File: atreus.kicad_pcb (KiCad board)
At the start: 2 copper layers, 111.8 x 87.6 mm, 45 parts

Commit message: Programmatically place repeated traces.
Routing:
- net N-row-2: track 173.4 -> 149.4 mm
- net N-diode-22: track 0.00 -> 18.8 mm
- net N-diode-20: track 14.1 -> 0.00 mm
- net N-diode-23: track 0.00 -> 13.5 mm
- net N-diode-21: track 12.0 -> 0.00 mm
- net N-col-4: track 119.4 -> 130.7 mm
- net N-col-1: track 182.1 -> 193.1 mm
- net N-col-5: track 67.0 -> 56.7 mm
- net N-col-0: track 207.2 -> 214.9 mm
- net N-row-0: track 132.1 -> 138.5 mm
- net N-col-3: track 155.4 -> 159.7 mm
- net N-row-1: track 121.1 -> 124.1 mm
- net N-col-2: track 177.2 -> 179.5 mm

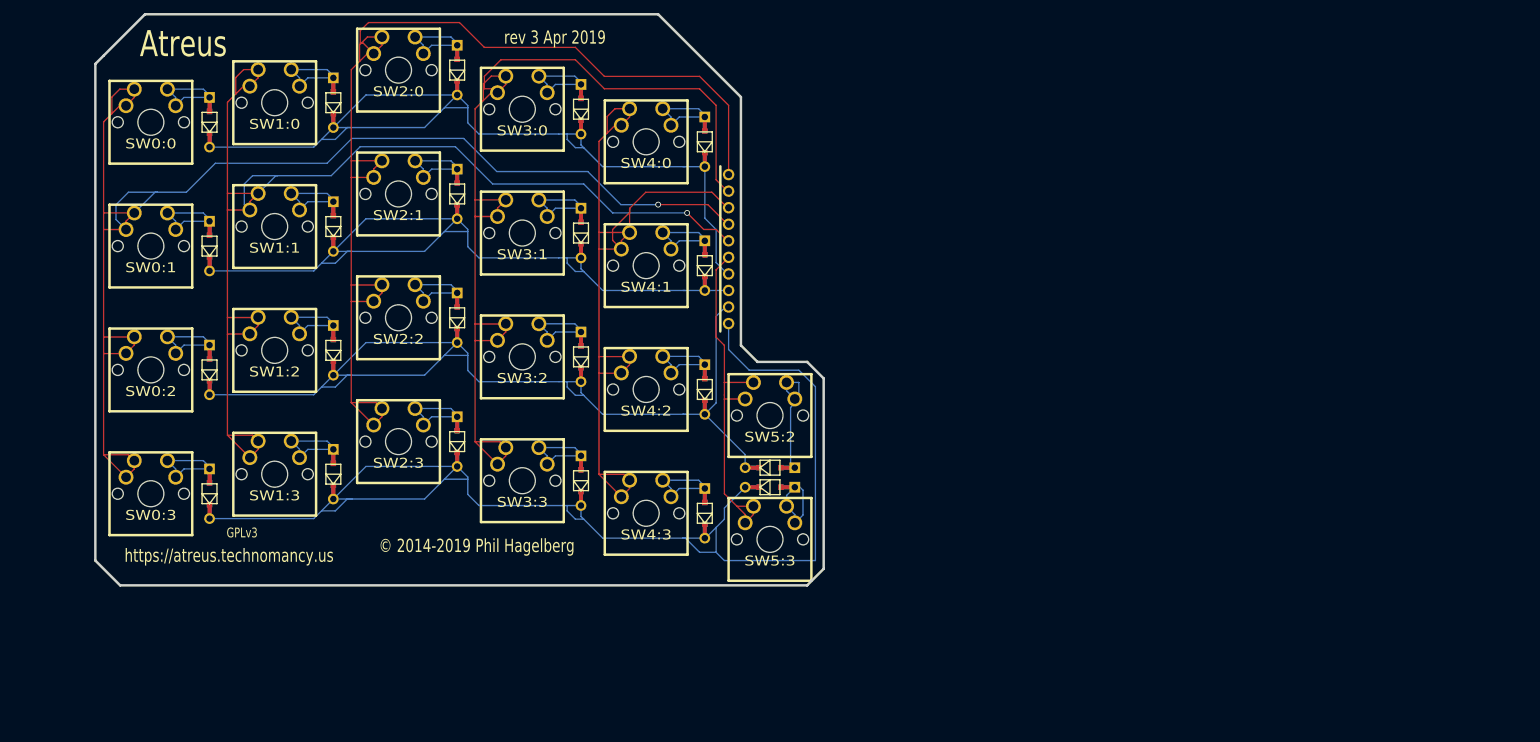
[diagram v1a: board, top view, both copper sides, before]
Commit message: Revert changes to create split PCB.
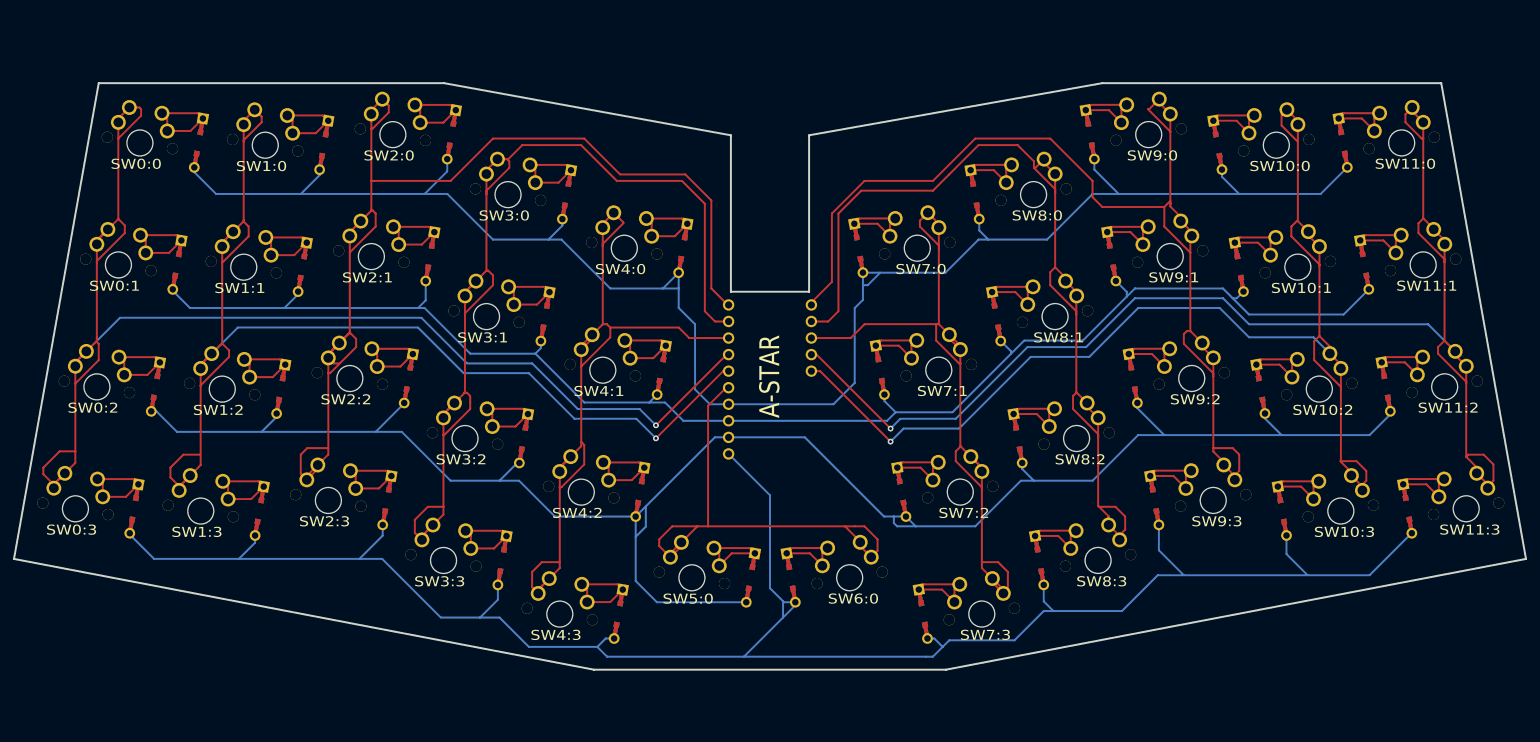
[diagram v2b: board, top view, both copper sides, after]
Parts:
- removed the D2:2 at (48.0, 28.0)
- removed the D2:2 at (86.0, 39.0)
- removed the D2:2 at (86.0, 58.0)
- removed the D2:2 at (86.0, 77.0)
- removed the D2:2 at (105.0, 26.0)
- removed the D2:2 at (105.0, 45.0)
- removed the D2:2 at (105.0, 64.0)
- removed the D2:2 at (105.0, 83.0)
- removed the D2:2 at (124.0, 31.0)
- removed the D2:2 at (124.0, 50.0)
- removed the D2:2 at (124.0, 69.0)
- removed the D2:2 at (48.0, 47.0)
- removed the D2:2 at (124.0, 88.0)
- removed the D2:2 at (134.0, 81.0)
- removed the D2:2 at (134.0, 84.0)
- removed the D2:2 at (48.0, 66.0)
- removed the D2:2 at (48.0, 85.0)
- removed the D2:2 at (67.0, 25.0)
- removed the D2:2 at (67.0, 44.0)
- removed the D2:2 at (67.0, 63.0)
- removed the D2:2 at (67.0, 82.0)
- removed the D2:2 at (86.0, 20.0)
- removed SW5:2, SW5:3: , MX_FLIP
- added D2:2: , DIODE, F.Cu at (46.3, 31.2)
- added D2:2: , DIODE, F.Cu at (81.8, 48.6)
- added D2:2: , DIODE, F.Cu at (78.5, 67.3)
- added D2:2: , DIODE, F.Cu at (75.2, 86.0)
- added D2:2: , DIODE, F.Cu at (102.8, 39.1)
- added D2:2: , DIODE, F.Cu at (99.5, 57.8)
- added D2:2: , DIODE, F.Cu at (96.2, 76.5)
- added D2:2: , DIODE, F.Cu at (92.9, 95.2)
- added D2:2: , DIODE, F.Cu at (120.6, 47.3)
- added D2:2: , DIODE, F.Cu at (117.3, 66.0)
- added D2:2: , DIODE, F.Cu at (114.0, 84.8)
- added D2:2: , DIODE, F.Cu at (43.0, 49.9)
- added D2:2: , DIODE, F.Cu at (110.7, 103.5)
- added D2:2: , DIODE, F.Cu at (131.0, 97.9)
- added D2:2: , DIODE, F.Cu at (137.2, 97.9)
- added D2:2: , DIODE, F.Cu at (147.6, 47.3)
- added D2:2: , DIODE, F.Cu at (150.9, 66.0)
- added D2:2: , DIODE, F.Cu at (154.2, 84.7)
- added D2:2: , DIODE, F.Cu at (157.5, 103.5)
- added D2:2: , DIODE, F.Cu at (165.4, 39.1)
- added D2:2: , DIODE, F.Cu at (168.7, 57.8)
- added D2:2: , DIODE, F.Cu at (172.0, 76.5)
- added D2:2: , DIODE, F.Cu at (39.7, 68.6)
- added D2:2: , DIODE, F.Cu at (175.3, 95.2)
- added D2:2: , DIODE, F.Cu at (183.1, 29.9)
- added D2:2: , DIODE, F.Cu at (186.4, 48.6)
- added D2:2: , DIODE, F.Cu at (189.7, 67.3)
- added D2:2: , DIODE, F.Cu at (193.0, 86.0)
- added D2:2: , DIODE, F.Cu at (202.7, 31.5)
- added D2:2: , DIODE, F.Cu at (206.0, 50.2)
- added D2:2: , DIODE, F.Cu at (209.3, 68.9)
- added D2:2: , DIODE, F.Cu at (212.6, 87.7)
- added D2:2: , DIODE, F.Cu at (221.9, 31.2)
- added D2:2: , DIODE, F.Cu at (36.4, 87.3)
- added D2:2: , DIODE, F.Cu at (225.2, 49.9)
- added D2:2: , DIODE, F.Cu at (228.5, 68.6)
- added D2:2: , DIODE, F.Cu at (231.8, 87.3)
- added D2:2: , DIODE, F.Cu at (65.6, 31.5)
- added D2:2: , DIODE, F.Cu at (62.3, 50.2)
- added D2:2: , DIODE, F.Cu at (59.0, 68.9)
- added D2:2: , DIODE, F.Cu at (55.7, 87.7)
- added D2:2: , DIODE, F.Cu at (85.1, 29.9)
- added SW10:0: , MX_FLIP, F.Cu at (211.7, 31.5)
- added SW10:1: , MX_FLIP, F.Cu at (215.0, 50.2)
- added SW10:2: , MX_FLIP, F.Cu at (218.3, 68.9)
- added SW10:3: , MX_FLIP, F.Cu at (221.6, 87.7)
- added SW11:0: , MX_FLIP, F.Cu at (230.9, 31.2)
- added SW11:1: , MX_FLIP, F.Cu at (234.2, 49.9)
- added SW11:2: , MX_FLIP, F.Cu at (237.5, 68.6)
- added SW11:3: , MX_FLIP, F.Cu at (240.8, 87.3)
- added SW5:0: , MX_FLIP, F.Cu at (122.0, 97.9)
- added SW6:0: , MX_FLIP, F.Cu at (146.2, 97.9)
- added SW7:0: , MX_FLIP, F.Cu at (156.6, 47.3)
- added SW7:1: , MX_FLIP, F.Cu at (159.9, 66.0)
- added SW7:2: , MX_FLIP, F.Cu at (163.2, 84.7)
- added SW7:3: , MX_FLIP, F.Cu at (166.5, 103.5)
- added SW8:0: , MX_FLIP, F.Cu at (174.4, 39.1)
- added SW8:1: , MX_FLIP, F.Cu at (177.7, 57.8)
- added SW8:2: , MX_FLIP, F.Cu at (181.0, 76.5)
- added SW8:3: , MX_FLIP, F.Cu at (184.3, 95.2)
- added SW9:0: , MX_FLIP, F.Cu at (192.1, 29.9)
- added SW9:1: , MX_FLIP, F.Cu at (195.4, 48.6)
- added SW9:2: , MX_FLIP, F.Cu at (198.7, 67.3)
- added SW9:3: , MX_FLIP, F.Cu at (202.0, 86.0)
- ?: value (none) -> A-STAR
- moved SW4:3 20.4 mm to (101.7, 103.5), turned to -10 degrees
- moved ? 20.0 mm to (134.0, 70.0)
- moved SW4:2 18.6 mm to (105.0, 84.8), turned to -10 degrees
- moved SW4:1 17.4 mm to (108.3, 66.0), turned to -10 degrees
- moved SW3:3 17.2 mm to (83.9, 95.2), turned to -10 degrees
- moved SW4:0 16.7 mm to (111.6, 47.3), turned to -10 degrees
- moved SW3:2 15.3 mm to (87.2, 76.5), turned to -10 degrees
- moved SW2:3 14.1 mm to (66.2, 86.0), turned to -10 degrees
- moved SW3:1 13.9 mm to (90.5, 57.8), turned to -10 degrees
- moved SW3:0 13.3 mm to (93.8, 39.1), turned to -10 degrees
- moved SW1:3 12.7 mm to (46.7, 87.7), turned to -10 degrees
- moved SW2:2 11.9 mm to (69.5, 67.3), turned to -10 degrees
- moved SW0:3 11.8 mm to (27.4, 87.3), turned to -10 degrees
- moved SW2:1 10.5 mm to (72.8, 48.6), turned to -10 degrees
- moved SW1:2 10.0 mm to (50.0, 68.9), turned to -10 degrees
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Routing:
- net N-col-10: track 0.00 -> 211.5 mm, vias 0 -> 1
- net N-col-9: track 0.00 -> 193.0 mm, vias 0 -> 1
- net N-col-8: track 0.00 -> 176.2 mm
- net N-col-7: track 0.00 -> 153.6 mm
- net N-row-2: track 149.4 -> 281.8 mm
- net N-row-0: track 138.5 -> 264.8 mm
- net N-col-6: track 0.00 -> 124.5 mm
- net N-row-1: track 124.1 -> 226.9 mm
- net N-row-3: track 202.3 -> 299.5 mm
- net N-col-5: track 56.7 -> 80.4 mm
- net N-diode-21: track 0.00 -> 15.9 mm
- net N-diode-32: track 0.00 -> 15.9 mm
- net N-diode-25: track 0.00 -> 15.9 mm
- net N-diode-38: track 0.00 -> 15.9 mm
- net N-diode-33: track 0.00 -> 15.9 mm
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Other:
- board size 111.8 x 87.6 mm -> 232 x 90 mm
- board text removed: "Atreus"
- board text removed: "GPLv3"
- board text removed: "https://atreus.technomancy.us"
- board text removed: "rev 3 Apr 2019"
- board text removed: "© 2014-2019 Phil Hagelberg"

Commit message: Fixed Edge.cuts layout so that the bottom switches are not cut in half
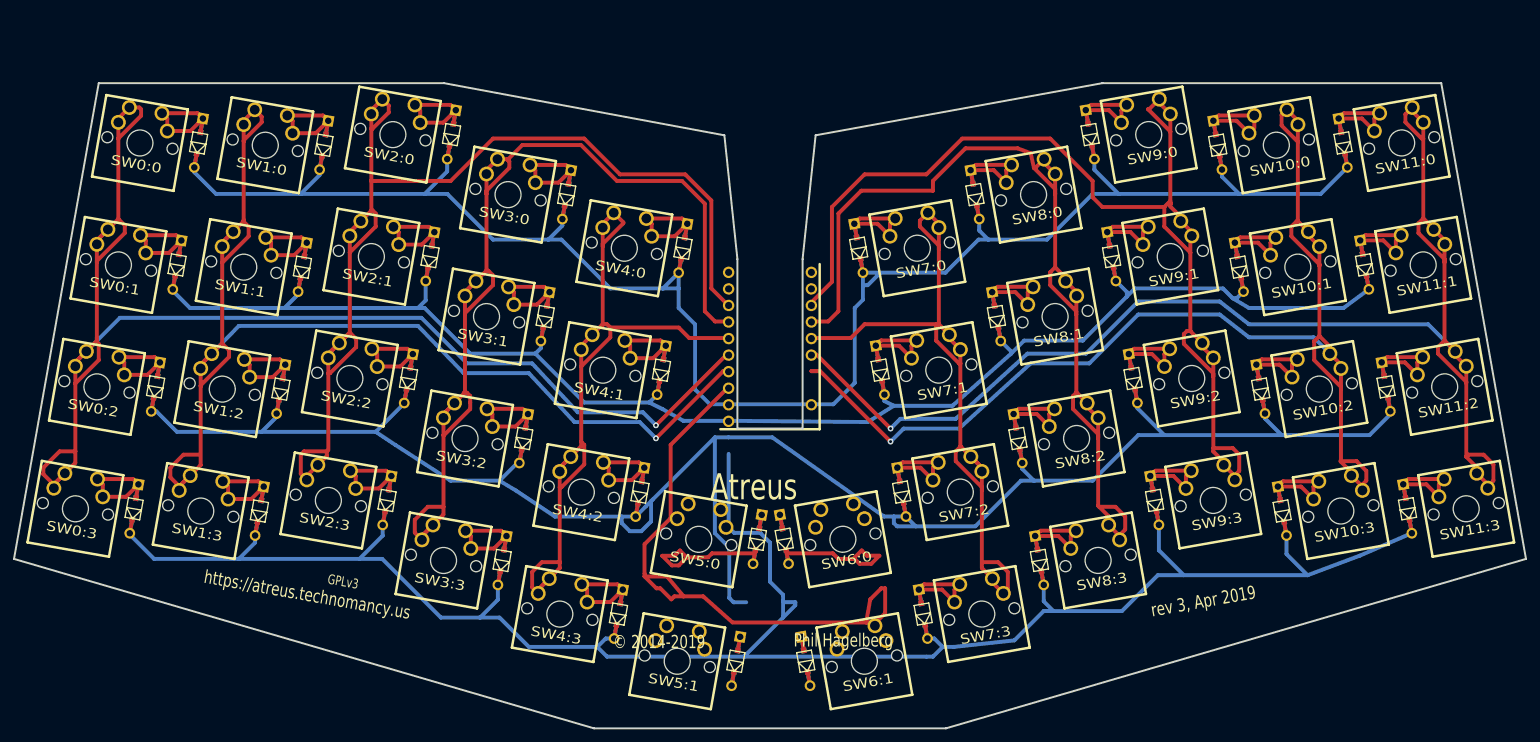
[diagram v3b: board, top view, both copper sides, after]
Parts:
- removed the D2:2 at (131.0, 97.9)
- removed the D2:2 at (137.2, 97.9)
- added D2:2: , DIODE, F.Cu at (132.1, 92.0)
- added D2:2: , DIODE, F.Cu at (128.8, 110.7)
- added D2:2: , DIODE, F.Cu at (136.2, 92.0)
- added D2:2: , DIODE, F.Cu at (139.5, 110.7)
- added SW5:1: , MX_FLIP, F.Cu at (119.8, 110.7)
- added SW6:1: , MX_FLIP, F.Cu at (148.5, 110.7)
- ?: value A-STAR -> (none)
- moved SW5:0 6.00 mm to (123.1, 92.0)
- moved SW6:0 6.00 mm to (145.2, 92.0)
- moved ? 5.00 mm to (134.0, 65.0)
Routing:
- net N-col-5: track 80.4 -> 92.9 mm
- net N-col-2: track 189.2 -> 183.7 mm
- net N-col-6: track 124.5 -> 119.2 mm
- net N-diode-20: track 15.9 -> 20.4 mm
- net N-diode-24: track 15.9 -> 20.3 mm
- net N-row-0: track 264.8 -> 261.4 mm
- net (no net): track 0.00 -> 3.46 mm
- net N-row-1: track 226.9 -> 223.8 mm
- net N-col-4: track 124.1 -> 121.2 mm
- net N-row-2: track 281.8 -> 283.8 mm
- net N-col-9: track 193.0 -> 191.6 mm
- net N-col-10: track 211.5 -> 210.6 mm
- net N-col-8: track 176.2 -> 176.8 mm
- net N-col-7: track 153.6 -> 154.2 mm
- net N-row-3: track 299.5 -> 300.1 mm
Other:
- board size 232 x 90 mm -> 232 x 99 mm
- board text added: "Atreus"
- board text added: "GPLv3"
- board text added: "Phil Hagelberg"
- board text added: "https://atreus.technomancy.us"
- board text added: "rev 3, Apr 2019"
- board text added: "© 2014-2019"
